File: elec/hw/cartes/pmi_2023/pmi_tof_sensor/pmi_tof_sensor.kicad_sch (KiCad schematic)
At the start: 40 parts, among them U1 SN74LVC1T45DBV, U2 TMF8821, U3 VL53L1CXV0FY1, U4 VL53L5CXV0GC

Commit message: pmi_tof_sensors schematicsupdate after review
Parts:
- added J1: tof_sensor_female, symbol cocotter_connectors:tof_sensor_female
- R10, R9: now not fitted
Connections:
- net +3.3V: now also J1.2 (P3V3)
- net DETECT_IRQ_3v3: now also J1.4 (detect_irq_3v3)
- net GND: now also J1.1 (GND)
- net SCL_3v3: now also J1.6 (SCL_3V3)
- net SDA_3v3: now also J1.5 (SDA)
- net enable_next_board_3v3: now also J1.3 (enable_next_board_3v3)
- net /enable_tof_3v3: now also J1.7 (/enable_tof_3v3)
- net /reset_tof_com_3v3: now also J1.8 (/reset_com_3v3)

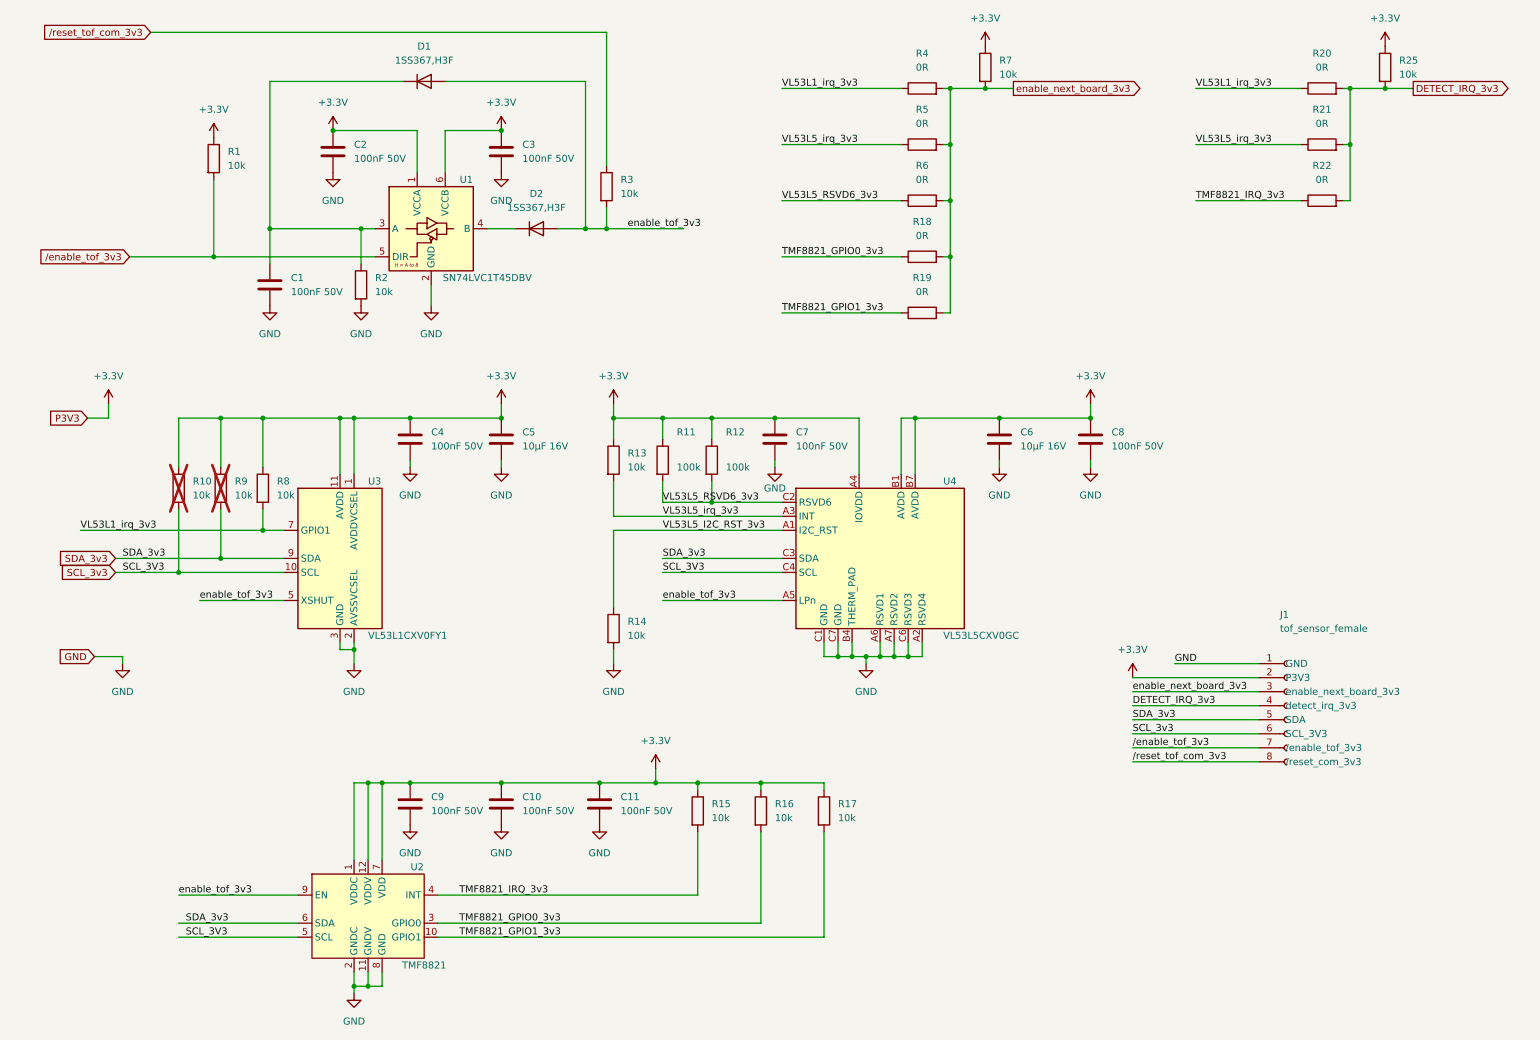
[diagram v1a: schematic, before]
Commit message: pmi_tof_sensor : last commit before tmf8821 deletion
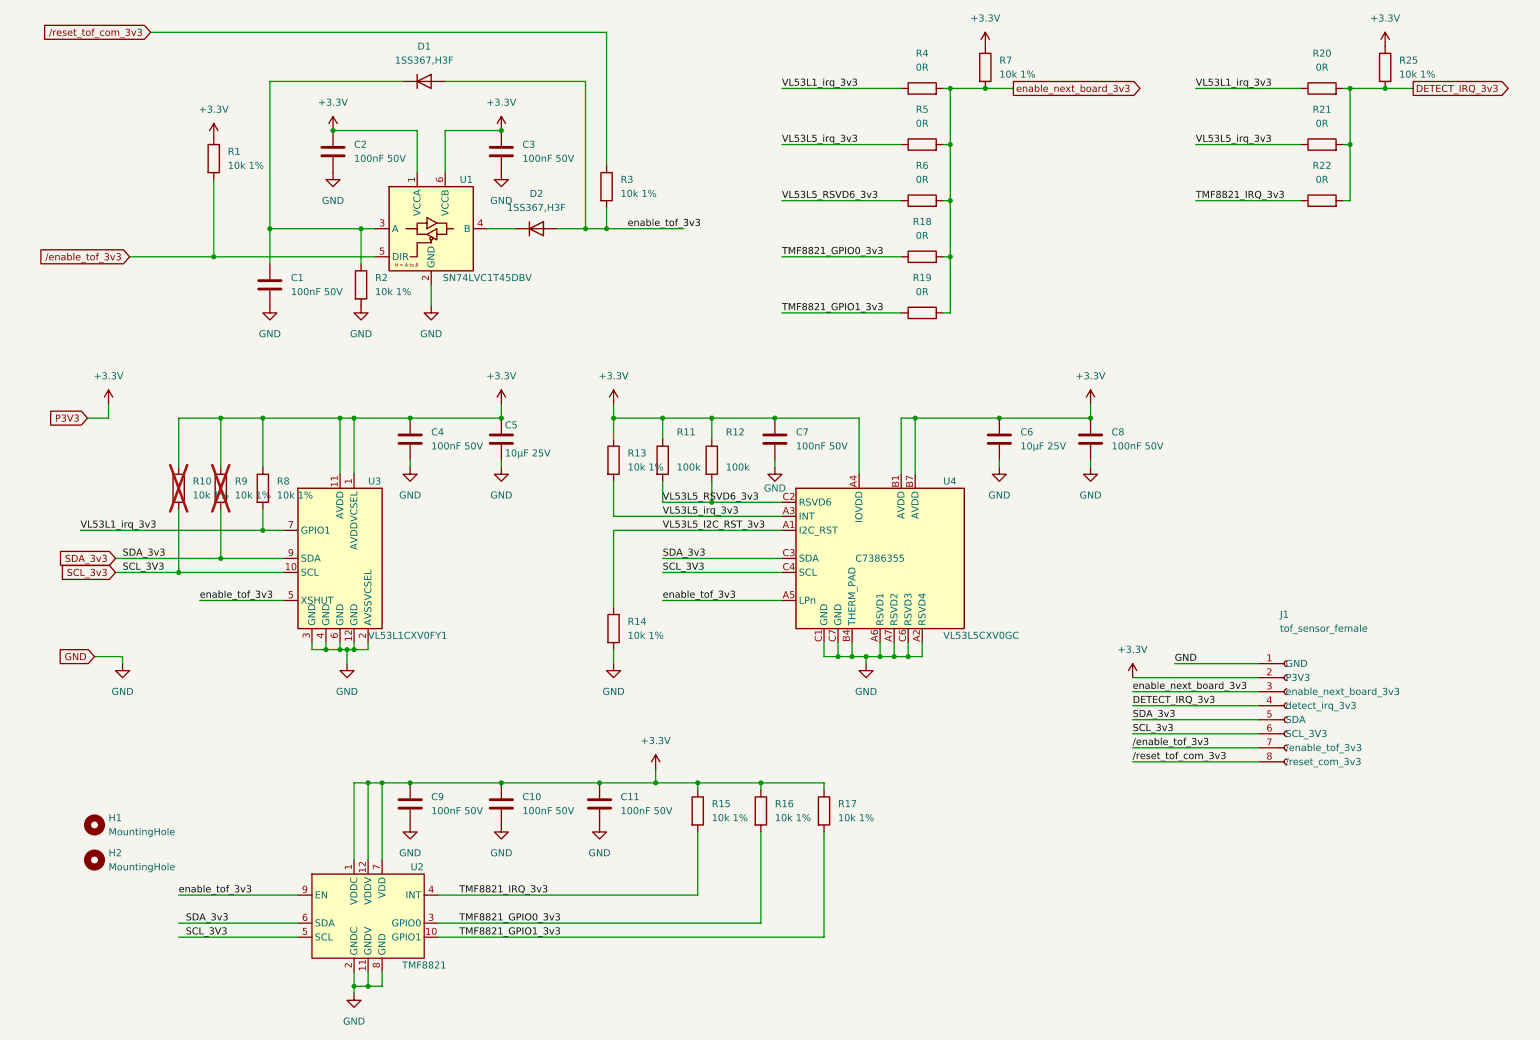
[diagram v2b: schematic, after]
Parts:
- added H1, H2: MountingHole, cocotter_others:MountingHole_2.1mm, symbol Mechanical:MountingHole
- C1, C10, C11, C2, C3, C4, C7, C8, C9: footprint (none) -> cocotter_capacitors:C_0603_1608Metric; JLCPCB (none) -> C14663
- C5, C6: value 10µF 16V -> 10µF 25V; footprint (none) -> cocotter_capacitors:C_0805_2012Metric; symbol cocotter_capacitors:C_10µF_16V_0805 -> cocotter_capacitors:C_10µF_25V_0805_X5R; JLCPCB (none) -> C15850; Specification 10µF 16V X7R 0805 -> 10µF 25V X7R 0805
- J1: footprint (none) -> cocotter_connectors:tof_sensor_female
- R1, R10, R13, R14, R15, R16, R17, R2, R25, R3, R7, R8, R9: value 10k -> 10k 1%; JLCPCB (none) -> C25804
- R11, R12: JLCPCB (none) -> C25803
- R18, R19, R20, R21, R22, R4, R5, R6: JLCPCB (none) -> C431718
- U1: JLCPCB (none) -> C7843
- U2: footprint (none) -> cocotter_ic:TMF882x
- U3: footprint Sensor_Distance:ST_VL53L1x -> cocotter_ic:ST_VL53L1x; JLCPCB (none) -> C190004
- U4: JLCPCB (none) -> C7386355

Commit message: pmi_tof_sensor : new form factor and enable sequencer
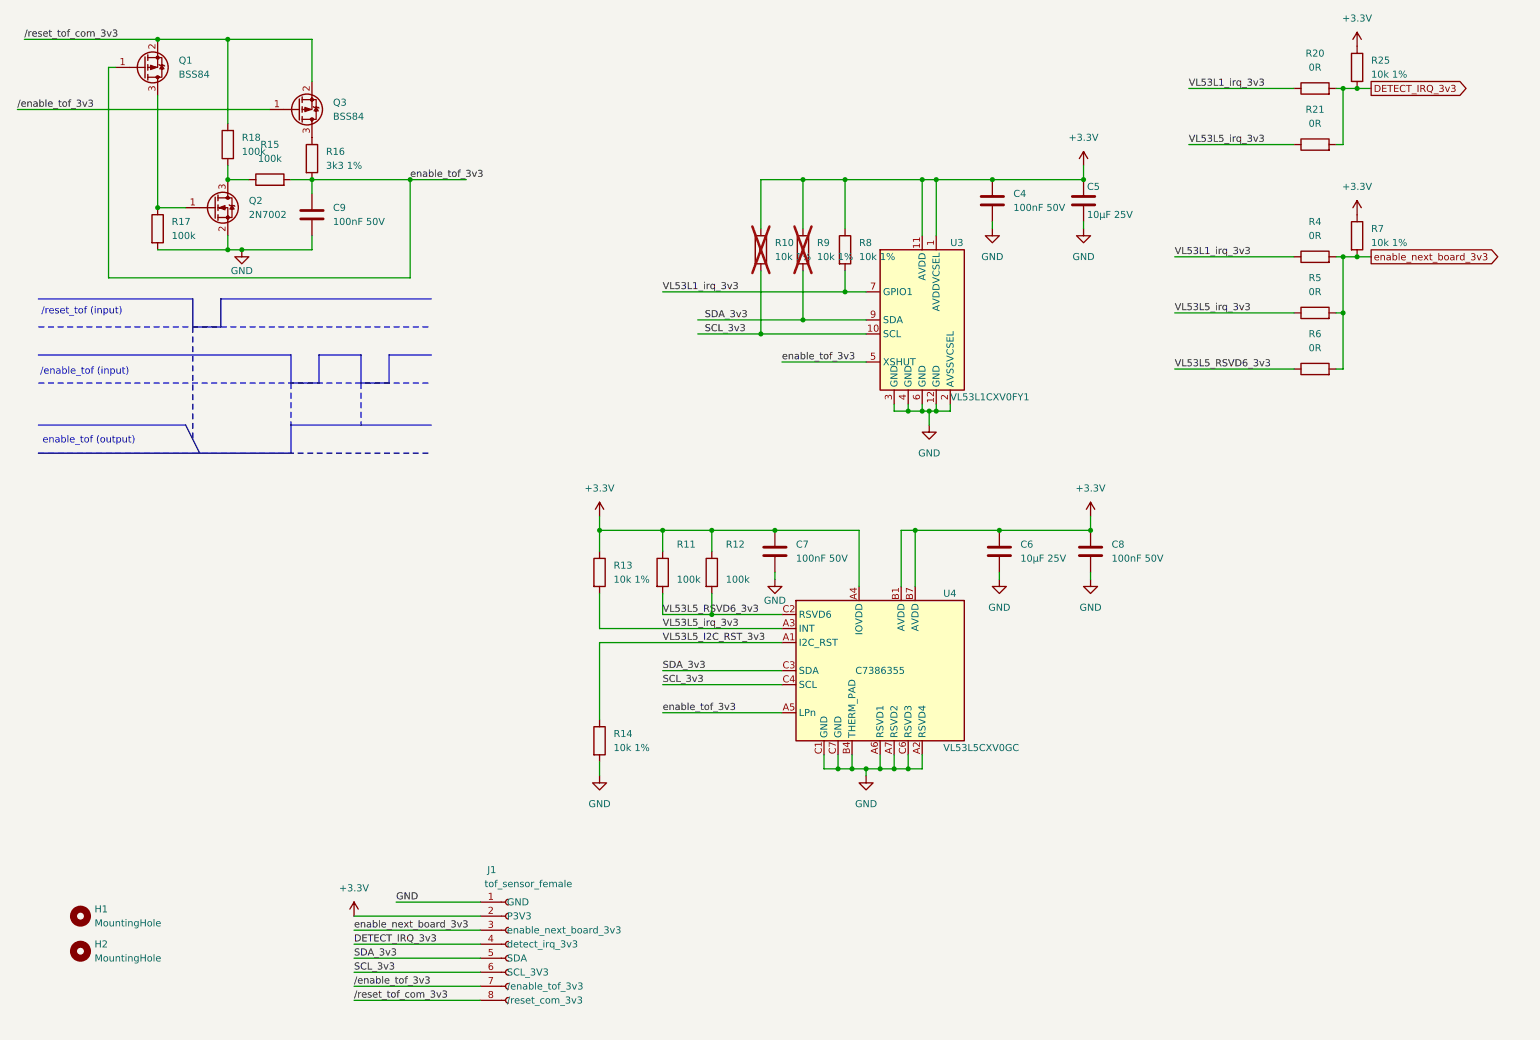
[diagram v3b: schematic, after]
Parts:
- removed C1, C10, C11, C2, C3: 100nF 50V, cocotter_capacitors:C_0603_1608Metric, symbol cocotter_capacitors:C_100nF_50V_0603
- removed D1, D2: 1SS367,H3F, Diode_SMD:D_SOD-323, symbol cocotter_diodes:1SS367,H3F
- removed R1, R15, R16, R17, R2, R3: 10k 1%, cocotter_resistor:r0603_reflow, symbol cocotter_resistors:R_10k_0603_1%
- removed R18, R19, R22: 0R, cocotter_resistor:r0603_reflow, symbol cocotter_resistors:R_0R_0603
- removed U1: SN74LVC1T45DBV, Package_TO_SOT_SMD:SOT-23-6, symbol cocotter_ic:SN74LVC1T45DBV
- removed U2: TMF8821, cocotter_ic:TMF882x, symbol cocotter_ic:TMF8821
- added Q1, Q3: BSS84, cocotter_transistors:SOT-23-3, symbol cocotter_transistors:BSS84
- added Q2: 2N7002, Package_TO_SOT_SMD:SOT-23, symbol cocotter_transistors:2N7002
- added R15, R17, R18: 100k, cocotter_resistor:r0603_reflow, symbol cocotter_resistors:R_100k_0603_1%
- added R16: 3k3 1%, cocotter_resistor:r0603_reflow, symbol cocotter_resistors:R_3k3_0603_1%
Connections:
- net +3.3V: no longer C9.1
- net GND: now also Q2.2 (S), R17.2
- net enable_tof_3v3: now also C9.1, Q1.1 (G), R15.2, R16.2
- net /enable_tof_3v3: now also Q3.1 (G)
- net /reset_tof_com_3v3: now also Q1.2 (S), Q3.2 (S), R18.2
- new net: Q2.3 (D), R15.1, R18.1
- new net: Q1.3 (D), Q2.1 (G), R17.1
- new net: Q3.3 (D), R16.1
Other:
- note added: "/enable_tof (input)"
- note added: "/reset_tof (input)"
- note added: "enable_tof (output)"
- moved on the sheet: C4, C5, C6, C7, C8, H1, H2, J1, R10, R11, R12, R13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

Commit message: modified rc constant of enable circuit
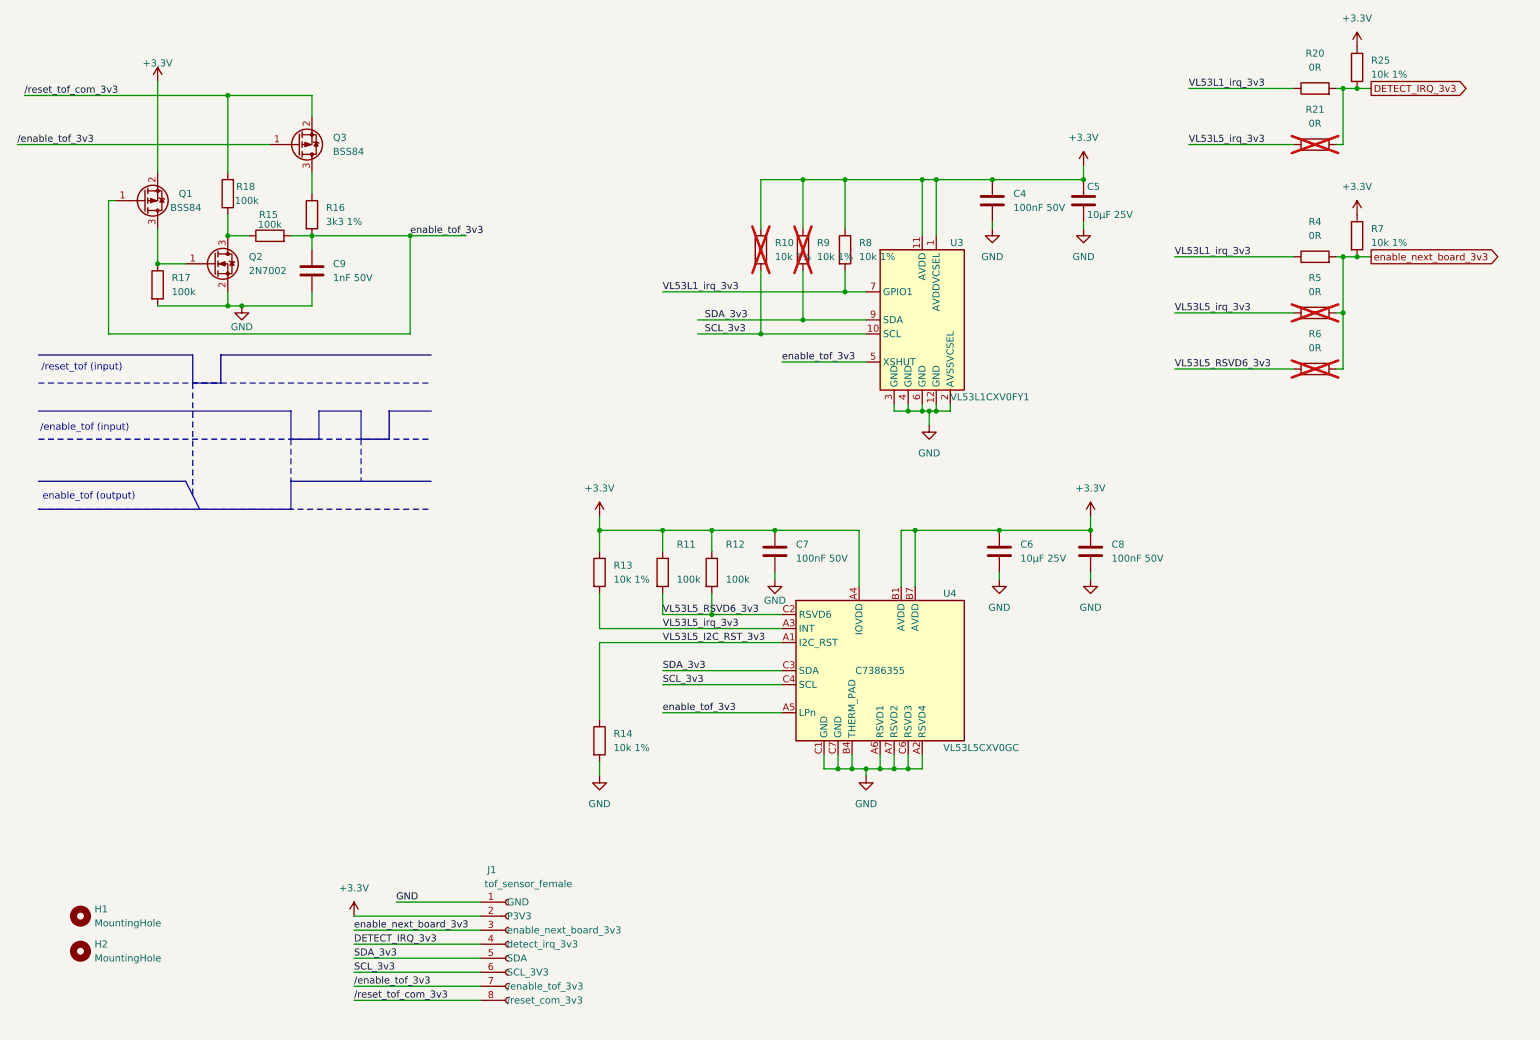
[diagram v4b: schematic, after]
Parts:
- C9: value 100nF 50V -> 1nF 50V; symbol cocotter_capacitors:C_100nF_50V_0603 -> cocotter_capacitors:C_1nF_50V_0603; JLCPCB C14663 -> C1588; Specification 100nF 50V X7R 0603 -> 1nF 50V X7R 0603
- Q2: footprint Package_TO_SOT_SMD:SOT-23 -> cocotter_transistors:SOT-23-3
- R21, R5, R6: now not fitted
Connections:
- net +3.3V: now also Q1.2 (S)
- net /reset_tof_com_3v3: no longer Q1.2 (S)
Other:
- moved on the sheet: C9, Q1, Q2, Q3, R15, R16, R17, R18

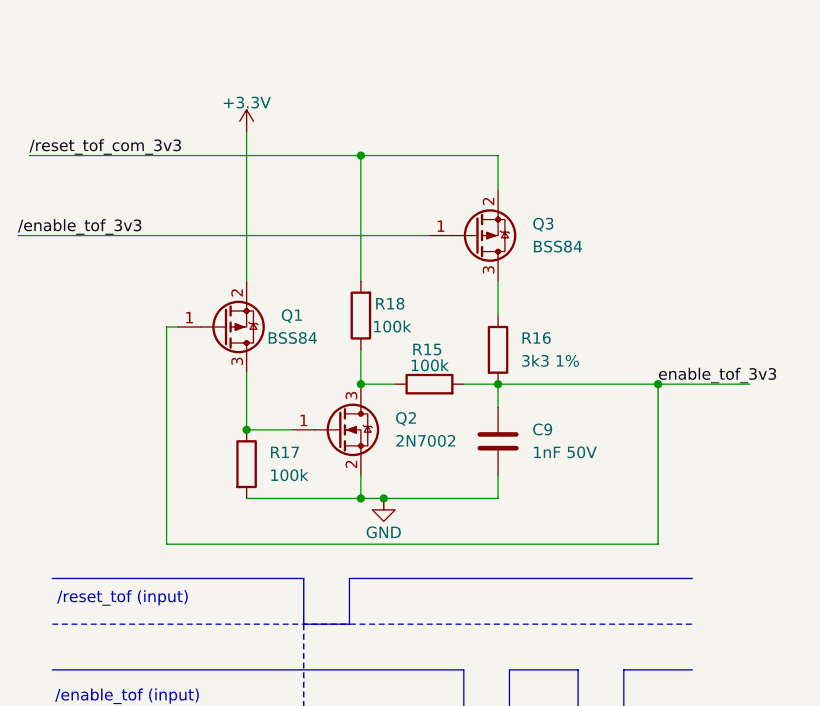
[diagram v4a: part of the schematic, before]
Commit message: modified mounting hole, replaced transistors to place them in bottom layer
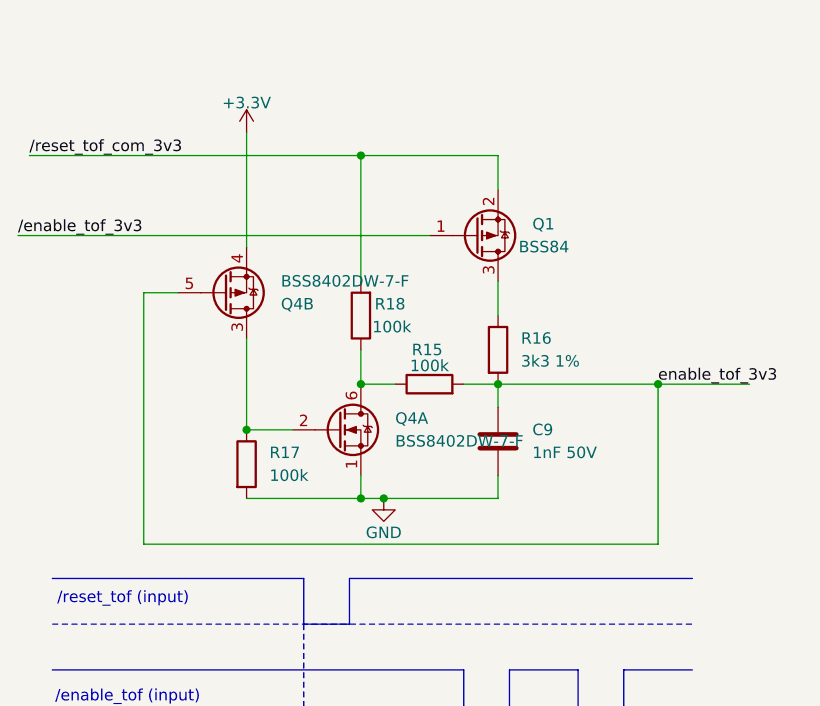
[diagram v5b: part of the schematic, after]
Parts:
- removed Q2: 2N7002, cocotter_transistors:SOT-23-3, symbol cocotter_transistors:2N7002
- removed Q3: BSS84, cocotter_transistors:SOT-23-3, symbol cocotter_transistors:BSS84
- added Q4: BSS8402DW-7-F, cocotter_transistors:SOT-363_SC-70-6, symbol cocotter_transistors:BSS8402DW-7-F
- H1, H2: footprint cocotter_others:MountingHole_2.1mm -> cocotter_others:MountingHole_2.5mm-slot_1mm
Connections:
- net +3.3V: now also Q4.4 (SP); no longer Q1.2 (S)
- net GND: now also Q4.1 (SN)
- net enable_tof_3v3: now also Q4.5 (GP); no longer Q1.1 (G)
- net /enable_tof_3v3: now also Q1.1 (G)
- net /reset_tof_com_3v3: now also Q1.2 (S)
- net at R15.1, R18.1: now also Q4.6 (DN)
- net at Q1.3 (D): now also R16.1; no longer R17.1
- new net: Q4.2 (GN), Q4.3 (DP), R17.1
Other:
- moved on the sheet: Q1
